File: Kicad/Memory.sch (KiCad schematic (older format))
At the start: 9 parts, among them U1 74LS593, U10 AT28C64B, U2 74LS593, U3 74HCT138, U5 74LS469, U6 74LS469, U7 74HCT574, U8 74HCT574, U9 CY628128E

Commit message: Made a slight update to the PCB layout.
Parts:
- U3: footprint Package_SO:SOIC-16_4.55x10.3mm_P1.27mm -> Package_SO:SOIC-16_3.9x9.9mm_P1.27mm
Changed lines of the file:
@@
 F 0 "U3" H 1550 7550 50  0000 C CNN
 F 1 "74HCT138" H 1550 7450 50  0000 C CNN
-F 2 "Package_SO:SOIC-16_4.55x10.3mm_P1.27mm" H 1800 6800 50  0001 C CNN
+F 2 "Package_SO:SOIC-16_3.9x9.9mm_P1.27mm" H 1800 6800 50  0001 C CNN
 F 3 "http://www.ti.com/lit/gpn/sn74LS138" H 1800 6800 50  0001 C CNN
 F 4 "Address Decode" H 1800 6800 50  0001 C CNN "Description"

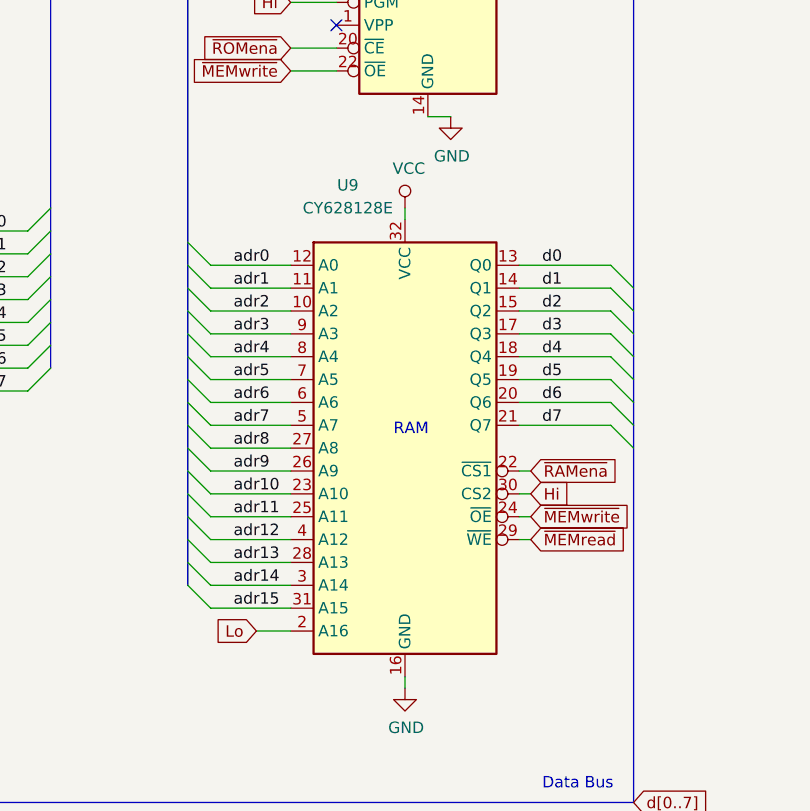
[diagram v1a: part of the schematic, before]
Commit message: Added the equ pseudo-op. Rearranged the PCB layout.
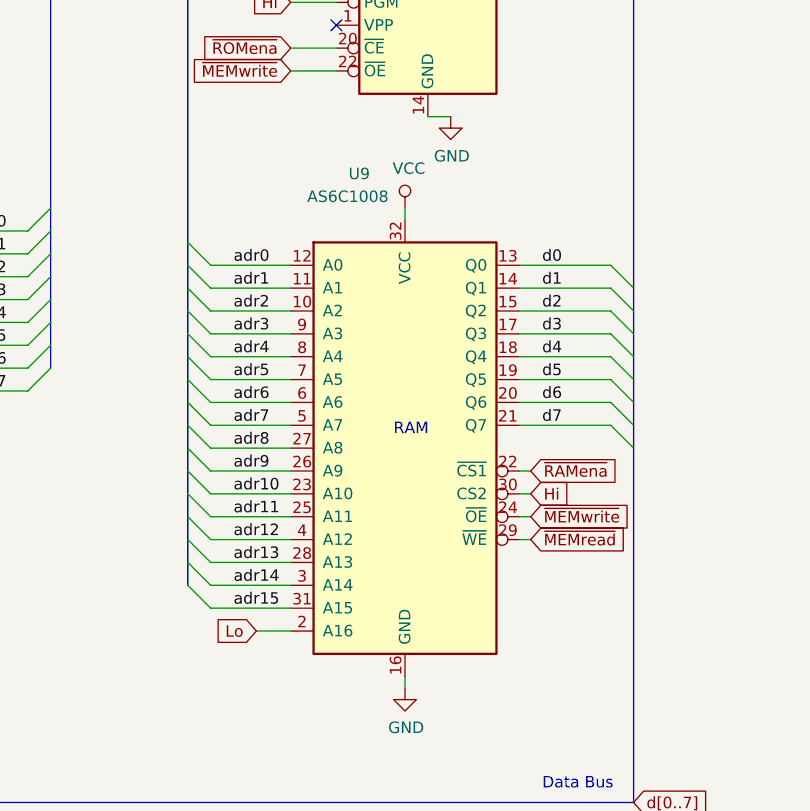
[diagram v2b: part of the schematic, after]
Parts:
- removed U9: CY628128E, Package_DIP:DIP-32_W15.24mm, symbol Memory_RAM:628128_DIP32_SSOP32
- added U9: AS6C1008, Package_DIP:DIP-32_W15.24mm_LongPads, symbol Memory_RAM:AS6C1008
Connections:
- net GND: now also U9.16 (GND)
- net Hi: now also U9.30 (CS2)
- net Lo: now also U9.2 (A16)
- net VCC: now also U9.32 (VCC)
- net adr0: now also U9.12 (A0)
- net adr1: now also U9.11 (A1)
- net adr10: now also U9.23 (A10)
- net adr11: now also U9.25 (A11)
- net adr12: now also U9.4 (A12)
- net adr13: now also U9.28 (A13)
- net adr14: now also U9.3 (A14)
- net adr15: now also U9.31 (A15)
- net adr2: now also U9.10 (A2)
- net adr3: now also U9.9 (A3)
- net adr4: now also U9.8 (A4)
- net adr5: now also U9.7 (A5)
- net adr6: now also U9.6 (A6)
- net adr7: now also U9.5 (A7)
- net adr8: now also U9.27 (A8)
- net adr9: now also U9.26 (A9)
- net d0: now also U9.13 (Q0)
- net d1: now also U9.14 (Q1)
- net d2: now also U9.15 (Q2)
- net d3: now also U9.17 (Q3)
- net d4: now also U9.18 (Q4)
- net d5: now also U9.19 (Q5)
- net d6: now also U9.20 (Q6)
- net d7: now also U9.21 (Q7)
- net ~MEMread: now also U9.29 (~WE)
- net ~MEMwrite: now also U9.24 (~OE)
- net ~RAMena: now also U9.22 (~CS1)
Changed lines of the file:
@@
 	8250 750  8950 750
 Connection ~ 5100 750
-$Comp
-L Memory_RAM:628128_DIP32_SSOP32 U9
-U 1 1 5E1BEA6F
-P 9200 4650
-F 0 "U9" H 8950 5800 50  0000 C CNN
-F 1 "CY628128E" H 8950 5700 50  0000 C CNN
-F 2 "Package_DIP:DIP-32_W15.24mm" H 9200 4650 50  0001 C CNN
-F 3 "http://www.futurlec.com/Datasheet/Memory/628128.pdf" H 9200 4650 50  0001 C CNN
-F 4 "RAM" H 9200 4650 50  0001 C CNN "Description"
-	1    9200 4650
-	1    0    0    -1
-$EndComp
 Wire Bus Line
 	5100 750  7650 750
@@
 	2500 2100 2350 2100
 Connection ~ 2500 2200
-Wire Bus Line
-	850  750  850  6600
-Wire Bus Line
-	3200 1700 3200 6200
-Wire Bus Line
-	5100 750  5100 4300
-Wire Bus Line
-	5700 1700 5700 6200
-Wire Bus Line
-	7650 750  7650 4300
-Wire Bus Line
-	10200 1400 10200 6200
-Wire Bus Line
-	8250 750  8250 5250
 Text Notes 2600 6850 0    50   ~ 0
 Low 8K is ROM,\nremainder is RAM
 Text Notes 7050 6950 0    50   ~ 0
 PC, SP and AR can write to the address bus which RAM and ROM reads.\nPC can only read from the address bus.\nSP and AR only read from the data bus.\nROM and RAM write to the data bus. RAM reads also!
+$Comp
+L Memory_RAM:AS6C1008 U9
+U 1 1 5EC8B164
+P 9200 3600
+F 0 "U9" H 9000 3750 50  0000 C CNN
+F 1 "AS6C1008" H 8950 3650 50  0000 C CNN
+F 2 "Package_DIP:DIP-32_W15.24mm_LongPads" H 9200 3600 50  0001 C CNN
+F 3 "" H 9200 3600 50  0001 C CNN
+	1    9200 3600
+	1    0    0    -1
+$EndComp
+Wire Bus Line
+	850  750  850  6600
+Wire Bus Line
+	3200 1700 3200 6200
+Wire Bus Line
+	5100 750  5100 4300
+Wire Bus Line
+	5700 1700 5700 6200
+Wire Bus Line
+	7650 750  7650 4300
+Wire Bus Line
+	10200 1400 10200 6200
+Wire Bus Line
+	8250 750  8250 5250
 $EndSCHEMATC

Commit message: Lots of changes.
I found a few wiring mistakes in the schematic and fixed them up.
I added microcode instructions to allow B to be copied out to A,
to the UART and to memory. I added a lot of `mem = mem op B`
instructions. I added some examples to test the above. I redid the
PCB layout and added copper pours.
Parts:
- U9: footprint Package_DIP:DIP-32_W15.24mm_LongPads -> Package_DIP:DIP-32_W15.24mm
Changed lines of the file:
@@
 encoding utf-8
 Sheet 2 5
-Title ""
-Date ""
+Title "FISC TTL CPU"
+Date "2020-05-21"
 Rev ""
 Comp ""
@@
 F 0 "U9" H 9000 3750 50  0000 C CNN
 F 1 "AS6C1008" H 8950 3650 50  0000 C CNN
-F 2 "Package_DIP:DIP-32_W15.24mm_LongPads" H 9200 3600 50  0001 C CNN
+F 2 "Package_DIP:DIP-32_W15.24mm" H 9200 3600 50  0001 C CNN
 F 3 "" H 9200 3600 50  0001 C CNN
 	1    9200 3600
